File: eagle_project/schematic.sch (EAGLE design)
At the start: 104 parts, among them IC1 AZ34063U, IC2 AZ34063U, IC3 AZ34063U, J1 USB-B, Q1 BC618, Q2 BC618, U1 MCP4912-E/SL, U2 OP07CSZ, U3 OP07CSZ, U4 MCP1501T-40E/CHY, U5 OP07CD, U6 OP07CD, U7 OP07CD

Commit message: schematic mostly done. added mp lab project
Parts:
- removed IC1: AZ34063U, IMPORTED_ELEMENTS:AZ34063U
- removed L3: 100uH, rcl:L-USWE-TPC
- removed L4: 1uH, IMPORTED:INDUCTOR
- removed Q2: BC618, transistor-npn:BC618
- added C21, C22, C23, C25, C26, C28, C29, C30, C31, C32, C38, C40: 100nF, rcl:C-EUC0805
- added C24, C27, C34, C39: 1uF, rcl:C-EUC0805
- added C33: 10uF, rcl:C-EUC0805
- added C35: 220uF/10V/105°, rcl:CPOL-EUE2.5-6
- added C36: 1n, rcl:C-EUC0805
- added C37: 100uF/10V/105°, rcl:CPOL-EUE2-5
- added C41, C42: 10n, rcl:C-EUC0805
- added D3, D4: BAS40, diode:BAS40
- added D5: SS13+, diode:SCHOTTKY-DIODESMC
- added D6, D7: 1N4148, diode:1N4148
- added F1: 1 A, special:FUSE
- added IC4, IC6: LM358A, linear:LM358D
- added IC5: PIC24FJ64GU202-I_SS, SamacSys_Parts:PIC24FJ64GU202-I_SS
- added IC7: AZ34063U, IMPORTED_ELEMENTS:AZ34063U
- added JP10, JP7: PINHD-2X4/90, Connector:PINHD-2X4/90
- added JP11: (no value), pinhead:PINHD-1X4
- added JP8: PINHD-1X5, Connector:PINHD-1X5
- added JP9: PINHD-2X6/90, Connector:PINHD-2X6/90
- added L7: 1mH, SamacSys_Parts:12LRS105C
- added L8: 1uH, IMPORTED:INDUCTOR
- added LED10, LED5, LED6, LED7, LED8, LED9: (no value), led:LEDCHIPLED_0805
- added LED4: (no value), led:LED3MM
- added OK1, OK2, OK4: TR 50%+, optocoupler:LTV816
- added OK3, OK5: ISP521-1X, optocoupler:LTV816
- added R101, R66: 470R, rcl:R-EU_R0805
- added R103, R68: 1K, rcl:R-EU_R0805
- added R104, R105, R62, R67, R70, R77, R78, R79, R81, R82, R84, R87, R97: 1k, rcl:R-EU_R0805
- added R51, R52: 100k 0.1%, rcl:R-EU_R0805
- added R55, R61, R64: 10k, rcl:R-EU_R0805
- added R56, R65: 2k4, rcl:R-EU_R2010
- added R57: 180k 0,1%, rcl:R-EU_R0805
- added R58: 68k 0,1%, rcl:R-EU_R0805
- added R59: 130R 0,1%, rcl:R-EU_R0805
- added R60: 500R, bourns:3362P
- added R69, R96: 160, rcl:R-EU_R0805
- added R71, R98: 510, rcl:R-EU_R0805
- added R72, R73, R74, R75, R76, R91, R92, R93, R94, R99: (no value), pot:TRIM_EU-S64W
- added R80, R95: 220, rcl:R-EU_R0805
- added R83, R85, R89, R90: 1.44k, rcl:R-EU_R0805
- added R86, R88: 3.88k, rcl:R-EU_R0805
- added S1: (no value), switch-omron:10-XX
- added S3: TL36PO, switch:TL36PO
- added T1, T2, T3, T4: (no value), transistor:MMBT3904LT1-NPN-SOT23-BEC
- added TP1, TP2, TP3, TP4, TP5: PTR1PAD1-13, testpad:PTR1PAD1-13
- added U11, U12, U8: OP07CD, IMPORTED:OP07CD
- added U14: MCP4912-E/SL, Microchip_By_element14_Batch_1:MCP4912-E/SL
- added X1, X2, X3: MKDSN1,5/4-5,08, con-phoenix-508:MKDSN1,5/4-5,08
- added X4, X5, X6, X7: MKDSN1,5/2-5,08, con-phoenix-508:MKDSN1,5/2-5,08
- added X8: MKDSN1,5/3-5,08, con-phoenix-508:MKDSN1,5/3-5,08
- C12: value 100uF -> 100uF/25V/105°
- C19, C20: value 1u -> 100nF; device resistor:CPOL-EUE2-5 -> rcl:C-EUC0805
- C3: value 100uF -> 100uF/10V/105°
- C4: value 470uF/10V/105°C+ FOOTPRINT -> 470uF/10V/105°C
- C5: value 100uF/10V/105° -> 220uF/10V/105°; device rcl:CPOL-EUE2-5 -> rcl:CPOL-EUE2.5-6
- C6: value 100nF -> 15pF
- C7: value 1000uF/25V/105° -> 15pF; device rcl:CPOL-EUE5-13 -> rcl:C-EUC0805
- C8: value 1n -> 10uF
- C9: value 100uF -> 10n; device rcl:CPOL-EUE2-5 -> rcl:C-EUC0805
- D1: value SS13+ -> 1N4148; device diode:SCHOTTKY-DIODESMC -> diode:1N4148
- JP1: value PINHD-1X5 -> (none); device Connector:PINHD-1X5 -> pinhead:PINHD-1X4
- JP2: value PINHD-1X5 -> (none); device Connector:PINHD-1X5 -> pinhead:PINHD-1X5
- JP3: value PINHD-2X6/90 -> (none); device Connector:PINHD-2X6/90 -> jumper:JP4E
- JP4: value PINHD-2X4/90 -> (none); device Connector:PINHD-2X4/90 -> jumper:JP4E
- JP5: value PINHD-2X6/90 -> PINHD-1X5; device Connector:PINHD-2X6/90 -> Connector:PINHD-1X5
- JP6: value PINHD-2X4/90 -> PINHD-2X6/90; device Connector:PINHD-2X4/90 -> Connector:PINHD-2X6/90
- L1, L5: value 100uH -> 1mH; device rcl:L-USWE-TPC -> SamacSys_Parts:12LRS105C
- LED2: device led:LED3MM -> led:LEDCHIPLED_0805
- Q1: value BC618 -> 16MHz; device transistor-npn:BC618 -> crystal:CRYSTALHC49U-V
- R10: value 1k -> 180k 0,1%; device resistor:R-EU_0207/7 -> rcl:R-EU_R0805
- R11: value 1k -> 68k 0,1%; device resistor:R-EU_0207/7 -> rcl:R-EU_R0805
- R12: value 1.44k -> 500R; device resistor:R-EU_0207/7 -> bourns:3362P
- R13: value 1k -> 137k; device resistor:R-EU_0207/7 -> rcl:R-EU_R0805
- R14: value 1.44k -> 1k; device resistor:R-EU_0207/7 -> bourns:3362P
- R15: value 1k -> 1M; device resistor:R-EU_0207/7 -> rcl:R-EU_R0805
- R16: value 3.88k -> 137k; device resistor:R-EU_0207/7 -> rcl:R-EU_R0805
- R17: value 160 -> 1k; device resistor:R-EU_0207/7 -> bourns:3362P
- R18: value 1k -> 150k; device resistor:R-EU_0207/7 -> rcl:R-EU_R0805
- R19: value 510 -> 82k; device resistor:R-EU_0207/7 -> rcl:R-EU_R0805
- R20: value 220 -> (none); device resistor:R-EU_0207/7 -> pot:TRIM_EU-S64W
- R21: value 1k -> 10k; device resistor:R-EU_0207/7 -> rcl:R-EU_R0805
- R22: device resistor:R-EU_0207/7 -> rcl:R-EU_R0805
- R23: value 1.44k -> 10k; device resistor:R-EU_0207/7 -> rcl:R-EU_R0805
- R24: value 1k -> (none); device resistor:R-EU_0207/7 -> rcl:R-EU_R0805
- R25: value 1.44k -> 3k3; device resistor:R-EU_0207/7 -> rcl:R-EU_R0805
- R26: value 1k -> 2k; device resistor:R-EU_0207/7 -> rcl:R-EU_R0805
- R27: value 3.88k -> 0R75; device resistor:R-EU_0207/7 -> rcl:R-EU_R0805
- R28: value 160 -> 47R; device resistor:R-EU_0207/7 -> rcl:R-EU_M0805
- R30: value (none) -> 100k; device rcl:R-EU_R0805 -> rcl:R-EU_M0805
- R31: value 33k -> 10k
- R32: value 3k9 -> 2k4; device rcl:R-EU_R0805 -> rcl:R-EU_R2010
- R33: value 0R24 -> 10k
- R34: value 75R -> 1k
- R38: value 0R24 -> 0R39
- R39: value 1k -> (none); device resistor:R-EU_0207/7 -> pot:TRIM_EU-S64W
- R40: value 510 -> 22k 0.1%; device resistor:R-EU_0207/7 -> rcl:R-EU_R0805
- R41: value (none) -> 91k 0.1%; device pot:TRIM_EU-S64W -> rcl:R-EU_R0805
- R43, R44, R45, R46, R49, R50: value (none) -> 100k 0.1%; device pot:TRIM_EU-S64W -> rcl:R-EU_R0805
- R47: value (none) -> 130R 0,1%; device pot:TRIM_EU-S64W -> rcl:R-EU_R0805
- R53: value 3k3 -> 10k
- R54: value 2k -> 3k3
- R63: value 1R5 -> 0R75
- R9: value 220 -> 1M; device resistor:R-EU_0207/7 -> rcl:R-EU_R0805
- U1: value MCP4912-E/SL -> OP07CD; device Microchip_By_element14_Batch_1:MCP4912-E/SL -> IMPORTED:OP07CD
- U2, U3: value OP07CSZ -> OP07CD; device Analog Devices_By_element14_Batch_1:OP07CSZ -> IMPORTED:OP07CD
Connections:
- removed net +5V1: C7.+, D1.C, L4.1, R31.2
- removed net D+: J1.3
- removed net D-: J1.2
- new net +5V3: C35.+, L5.2, L8.1, R25.2
- new net 1,451: IC4A.+IN, IC4B.+IN, TP5.TP, U1.IN-, U1.OUT
- new net AREF_3,3: D3.C, D4.C, IC5.PGED3/VREF+/CVREF+/AN0/C3INC/RP26/ASDA1/RA0, TP3.TP, U11.IN-, U11.OUT
- new net COM: OK3.EMIT, OK5.EMIT, X8-3.KL
- new net COM_IN_1_3,3: JP11.4
- new net COM_IN_2_3,3: JP1.4
- new net D+_PGD: IC5.PGED2/RP10/D+/RB10, J1.3, JP2.4
- new net D-_PGC: IC5.PGEC2/RP11/D-/RB11, J1.2, JP2.5
- new net D_IN_0: IC5.AN4/C1INB/RP2/SDA2/RB2, LED2.C, OK4.COL, R31.1
- new net D_IN_1: IC5.AN5/C1INA/RP3/SCL2/RB3, LED5.C, OK1.COL, R55.1
- new net D_IN_2: IC5.SOSCI/C2IND/RP4/RB4, LED6.C, OK2.COL, R64.1
- new net D_OUT_0: IC5.SOSCO/SCLKI/C2INC/PWRLCLK/RA4, T1.B
- new net D_OUT_1: IC5.TMS/RP5/USBID/RB5, T2.B
- new net I_IN_0_3,3: D3.A, IC5.PGED1/AN2/LVDIN/C2INB/RP0/RB0, JP11.1, R46.2, U8.OUT
- new net I_IN_1_+: JP4.3, X1-1.KL
- new net I_IN_1_-: X1-2.KL
- new net I_IN_1_3,3: D4.A, IC5.PGEC1/AN1-/AN3/C2INA/RP1/RB1, JP1.1, R52.2, U12.OUT
- new net I_IN_2_+: JP3.3, X1-3.KL
- new net I_IN_2_-: X1-4.KL
- new net MCLR: IC5.!MCLR, JP2.1, R23.1, S1.S, S1.S1
- new net N$100: JP9.8, R93.A, R93.S
- new net N$101: JP9.10, R94.A, R94.S
- new net N$102: R83.1, R92.E
- new net N$103: R85.1, R93.E
- new net N$104: R86.1, R94.E
- new net N$105: JP6.8, R74.A, R74.S
- new net N$106: JP6.10, R75.A, R75.S
- new net N$107: R73.E, R90.1
- new net N$108: R74.E, R89.1
- new net N$109: R99.E, U2.OFFSETN1
- new net N$110: R75.E, R88.1
- new net N$111: R76.A, U3.OFFSETN2
- new net N$112: R76.E, U3.OFFSETN1
- new net N$113: OK5.A, R101.2
- new net N$114: OK5.COL, X8-2.KL
- new net N$116: LED8.A, R103.1
- new net N$117: C33.1, IC5.VCAP
- new net N$118: LED8.C, OK5.C, T2.C
- new net N$119: LED9.A, R104.1
- new net N$120: LED10.A, R105.1
- new net N$65: U3.IN-
- new net N$66: U14.VOUTB, U2.IN-
- new net N$67: R97.1, T4.B
- new net N$68: JP7.4, R96.1, T4.E
- new net N$71: JP6.3, R79.1, R95.2
- new net N$72: JP6.7, R77.1, R89.2
- new net N$73: JP6.9, R87.1, R88.2
- new net N$74: JP6.5, R78.1, R90.2
- new net N$75: JP7.1, U3.IN+
- new net N$76: JP6.1, JP7.3
- new net N$77: JP6.2, JP7.5
- new net N$78: JP7.6, R97.2
- new net N$79: R72.E, R95.1
- new net N$80: JP6.6, R73.A, R73.S
- new net N$81: JP6.4, R72.A, R72.S
- new net N$84: R70.1, T3.B
- new net N$85: JP10.4, R69.1, T3.E
- new net N$86: JP9.3, R80.2, R84.1
- new net N$87: JP9.7, R81.1, R85.2
- new net N$88: JP9.9, R67.1, R86.2
- new net N$89: JP4.2, R45.2, R59.2
- new net N$90: JP9.5, R82.1, R83.2
- new net N$91: JP10.1, U2.IN+
- new net N$92: JP10.3, JP9.1
- new net N$93: IC6B.-IN, IC6B.OUT, R57.1
- new net N$94: JP10.5, JP9.2
- new net N$95: JP10.6, R70.2
- new net N$96: R43.1, R59.1
- new net N$97: R80.1, R91.E
- new net N$98: JP9.6, R92.A, R92.S
- new net N$99: JP9.4, R91.A, R91.S
- new net OSCI: C6.1, IC5.OSCI/CLKI/C1IND/RA2, Q1.1
- new net OSCO: C7.1, IC5.OSCO/CLKO/C2IND/RA3, Q1.2
- new net PROG: R105.2, S3.O
- new net RUN: R104.2, S3.S
- new net VBUS: IC5.VBUS/RB6, R28.2, R30.2
- new net VCC: R101.1, R103.2, R66.1, R68.2, S3.P
- new net VDD2: C38.1
- new net V_IN_-10-+10_0_3,3: IC4A.OUT, IC5.CVREF/AN6/C3INB/RP14/RB14, JP1.3, JP11.3, R17.2, R17.3
- new net V_IN_-10-+10_1_3,3: IC4B.OUT, IC5.AN7/C1INC/RP13/_RB13, R14.2, R14.3
- new net V_IN_0-10_0_3,3: IC5.PGEC3/CVREF-/AN1/C3IND/RP27/ASCL1/RA1, JP1.2, JP11.2, R10.2, R12.1
- new net V_IN_0-10_1_3,3: IC5.AN9/C3INA/RP15/RB15, R57.2, R60.1
- new net V_IN_1_-10-+10_+: R15.1, X2-1.KL
- new net V_IN_1_0-10_+: IC6A.+IN, X3-1.KL
- new net V_IN_2_-10-+10_+: R9.1, X2-3.KL
- new net V_IN_2_0-10_+: IC6B.+IN, X3-3.KL
- net +12V: now also C2.1, C22.1, C26.1, C28.1, C31.1, C39.1, C4.+, F1.2, IC2.VCC, IC3.VCC, IC4P.V+, IC6P.V+, IC7.VCC, JP3.4, JP4.4, R27.1, R38.1, R63.1, R71.1, R76.S, R98.1, R99.S, U2.VCC+, U3.VCC+; no longer C9.+, L4.2, R19.1, R30.2, R40.1, U2.V+, U3.V+
- net +3V3: now also C37.+, C40.1, C8.1, IC5.AVDD/VDD, IC5.VDD, IC5.VUSB3V3, JP2.2, L8.2, R23.2, R24.2; no longer C3.+, L2.2, R29.2
- net +5V: now also C41.1, C42.1, C9.1, OK1.A, OK2.A, OK4.A, R21.2, R22.2, R31.2, R33.2, R34.2, R55.2, R61.2, R62.2, R64.2, X5-1.KL, X6-1.KL, X7-1.KL
- net -12V: now also C25.1, C29.1, C32.1, IC4P.V-, U2.VCC-, U3.VCC-; no longer U2.V-, U3.V-
- net 2,577: now also R67.2, R87.2, TP2.TP; no longer R15.1, R26.1
- net 3,472: now also R78.2, R82.2, TP1.TP; no longer R11.1, R22.1
- net 4,096: now also R18.2, R40.2, TP4.TP, U14.VREFA, U14.VREFB; no longer U1.VREFA, U1.VREFB
- net CS_DAC1: now also IC5.TDO/C1INC/C2INC/C3INC/RP9/SDA1/_T1CK/RB9, U14.*CS; no longer U1.*CS
- net GND: now also C19.1, C20.1, C21.1, C22.2, C23.1, C24.2, C25.2, C26.2, C27.2, C28.2, C29.2, C30.2, C31.2, C32.2, C33.2, C34.2, C35.-, C36.2, C37.-, C38.2, C39.2, C40.2, C7.2, D5.A, IC5.AVSS/VSS, IC5.VSS_1, IC5.VSS_2, IC6P.V-, IC7.GND, JP10.7, JP10.8, JP2.3, JP3.1, JP4.1, JP6.11, JP6.12, JP7.7, JP7.8, JP9.11, JP9.12, L7.2, LED10.C, LED4.C, LED9.C, OK1.EMIT, OK2.EMIT, OK4.EMIT, R11.2, R19.1, R26.1, R30.1, R41.1, R44.1, R50.1, R58.2, R69.2, R77.2, R79.2, R81.2, R84.2, R96.2, S1.P, S1.P1, T1.E, T2.E, U1.VCC-, U11.VCC-, U12.VCC-, U14.*LDAC, U14.VSS, U8.VCC-, X2-2.KL, X2-4.KL, X3-2.KL, X3-4.KL, X4-2.KL; no longer C19.-, C20.-, C7.-, C9.-, IC1.GND, IC1.SWE, JP3.11, JP3.12, JP4.7, JP4.8, JP5.11, JP5.12, JP6.7, JP6.8, L5.2, LED2.C, R10.1, R13.1, R17.1, R21.1, R24.1, R28.1, R32.1, U1.*LDAC, U1.VSS
- net I+: now also C24.1, C27.1, JP5.1, JP8.1, R71.2, R98.2; no longer C19.+, C20.+, JP1.1, JP2.1, R19.2, R40.2
- net I-: now also JP5.2, JP8.2, T3.C, T4.C; no longer JP1.2, JP2.2, Q1.C, Q2.C
- net MOSI: now also IC5.TCK/RP8/SCL1/!USBOEN!/RB8, U14.SDI; no longer U1.SDI
- net N$11: now also LED4.A, R24.1; no longer JP3.3, R10.2, R9.1
- net N$12: now also C34.1, J1.1, R28.1; no longer JP3.7, R13.2, R14.1
- net N$13: now also C9.2, D1.A, OK4.C, R21.1; no longer JP3.9, R15.2, R16.1
- net N$14: now also R16.2, R17.1; no longer JP3.5, R11.2, R12.1
- net N$16: now also R22.1; no longer R30.1
- net N$17: now also R32.1, X5-2.KL; no longer IC1.COMP_INV_IN, R31.1, R32.2
- net N$18: now also OK3.A, R66.2; no longer IC1.IPK_SENSE, L3.1, R33.2, R34.1
- net N$20: now also IC4A.-IN, R15.2, R16.1; no longer U1.VOUTA, U2.+IN
- net N$21: now also D1.C, R32.2; no longer C8.1, IC1.TC
- net N$22: now also F1.1, X4-1.KL; no longer Q1.B, R18.2
- net N$23: now also R18.1, R19.2, U1.IN+; no longer JP3.4, R45.A, R45.S
- net N$24: now also R20.A, U1.OFFSETN2; no longer U1.VOUTB, U3.+IN
- net N$25: now also IC6A.-IN, IC6A.OUT, R10.1; no longer JP4.4, Q1.E, R17.2
- net N$26: now also R11.1, R12.2, R12.3; no longer JP3.6, R46.A, R46.S
- net N$27: now also R20.E, U1.OFFSETN1; no longer JP3.8, R47.A, R47.S
- net N$28: now also IC4B.-IN, R13.1, R9.2; no longer JP3.10, R48.A, R48.S
- net N$29: now also C41.2, D6.A, OK1.C, R33.1; no longer IC1.DRVC, R34.2
- net N$30: now also LED5.A, R34.1; no longer D1.A, IC1.SWC, L3.2
- net N$32: now also IC7.COMP_INV_IN, R25.1, R26.2; no longer JP4.1, U2.-IN
- net N$35: now also R13.2, R14.1; no longer JP3.1, JP4.3
- net N$36: now also R56.1, X6-2.KL; no longer JP3.2, JP4.5
- net N$37: now also OK3.COL, X8-1.KL; no longer Q2.B, R39.2
- net N$38: now also IC7.DRVC, IC7.IPK_SENSE, IC7.SWC, R27.2; no longer JP6.4, Q2.E, R28.2
- net N$39: now also D6.C, R56.2; no longer JP5.3, R20.1, R21.2
- net N$40: now also R40.1, R41.2, U11.IN+; no longer JP4.6, R18.1
- net N$41: now also R39.A, U8.OFFSETN2; no longer JP5.7, R24.2, R25.1
- net N$42: now also L7.1; no longer L5.1
- net N$43: now also R39.E, U8.OFFSETN1; no longer JP5.9, R26.2, R27.1
- net N$44: now also R42.A, U11.OFFSETN2; no longer JP5.5, R22.2, R23.1
- net N$45: now also R42.E, U11.OFFSETN1; no longer JP5.8, R43.A, R43.S
- net N$46: now also R45.1, R46.1, U8.IN-; no longer R23.2, R41.E
- net N$47: now also R43.2, R44.2, U8.IN+; no longer R45.E, R9.2
- net N$48: now also JP3.2, R47.2, R51.2; no longer R49.A, U3.VOS_TRIM
- net N$49: now also R47.1, R49.1; no longer JP6.1, U3.-IN
- net N$50: now also R48.A, U12.OFFSETN2; no longer JP5.1, JP6.3
- net N$51: now also R48.E, U12.OFFSETN1; no longer JP5.2, JP6.5
- net N$52: now also R51.1, R52.1, U12.IN-; no longer JP6.6, R39.1
- net N$53: now also R49.2, R50.2, U12.IN+; no longer R20.2, R42.E
- net N$54: now also C42.2, D7.A, OK2.C, R61.1; no longer JP5.6, R41.A, R41.S
- net N$55: now also R58.1, R60.2, R60.3; no longer JP5.4, R42.A, R42.S
- net N$56: now also LED6.A, R62.1; no longer R25.2, R43.E
- net N$57: now also R65.1, X7-2.KL; no longer JP5.10, R44.A, R44.S
- net N$58: now also D5.C, IC7.SWE, L5.1; no longer R27.2, R44.E
- net N$59: now also R99.A, U2.OFFSETN2; no longer R49.E, U3.VOS_TRIM_2
- net N$60: now also C36.1, IC7.TC; no longer R50.A, U2.VOS_TRIM
- net N$61: now also D7.C, R65.2; no longer R50.E, U2.VOS_TRIM_2
- net N$62: now also LED7.A, R68.1; no longer R12.2, R46.E
- net N$63: now also LED7.C, OK3.C, T1.C; no longer R14.2, R47.E
- net N$64: now also U14.VOUTA; no longer R16.2, R48.E
- net SCK: now also IC5.TDI/RP7/INT0/RB7, U14.SCK; no longer U1.SCK
- net V+: now also JP10.2, JP5.3, JP7.2, JP8.3; no longer JP1.3, JP2.3, JP4.2, JP6.2
- net V-: now also JP5.4, JP5.5, JP8.4, JP8.5; no longer JP1.4, JP1.5, JP2.4, JP2.5
- net VDD: now also C19.2, C20.2, C21.2, C23.2, C3.+, C30.1, L2.2, R20.S, R29.2, R39.S, R42.S, R48.S, U1.VCC+, U11.VCC+, U12.VCC+, U14.*SHDN, U14.VDD, U8.VCC+; no longer C2.1, C4.+, C6.1, IC1.VCC, IC2.VCC, IC3.VCC, J1.1, R33.1, R38.1, R49.S, R50.S, R63.1, U1.*SHDN, U1.VDD
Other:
- note added: "-10...10 V"
- note added: "0...10 V"
- note added: "0...20 mA"
- note added: "1"
- note added: "1P3T"
- note added: "2"
- note added: "3"
- note added: "4"
- note added: "IZHOD"
- note added: "Izbira napetostnega območja 2P4T"
- note added: "Izbira tok ali napetost 2P2T"
- note added: "Loop-powered"
- note added: "Samo upor"
- note added: "max +/- 12V"
- note added: "max +12V"
- note added: "max 24 mA"

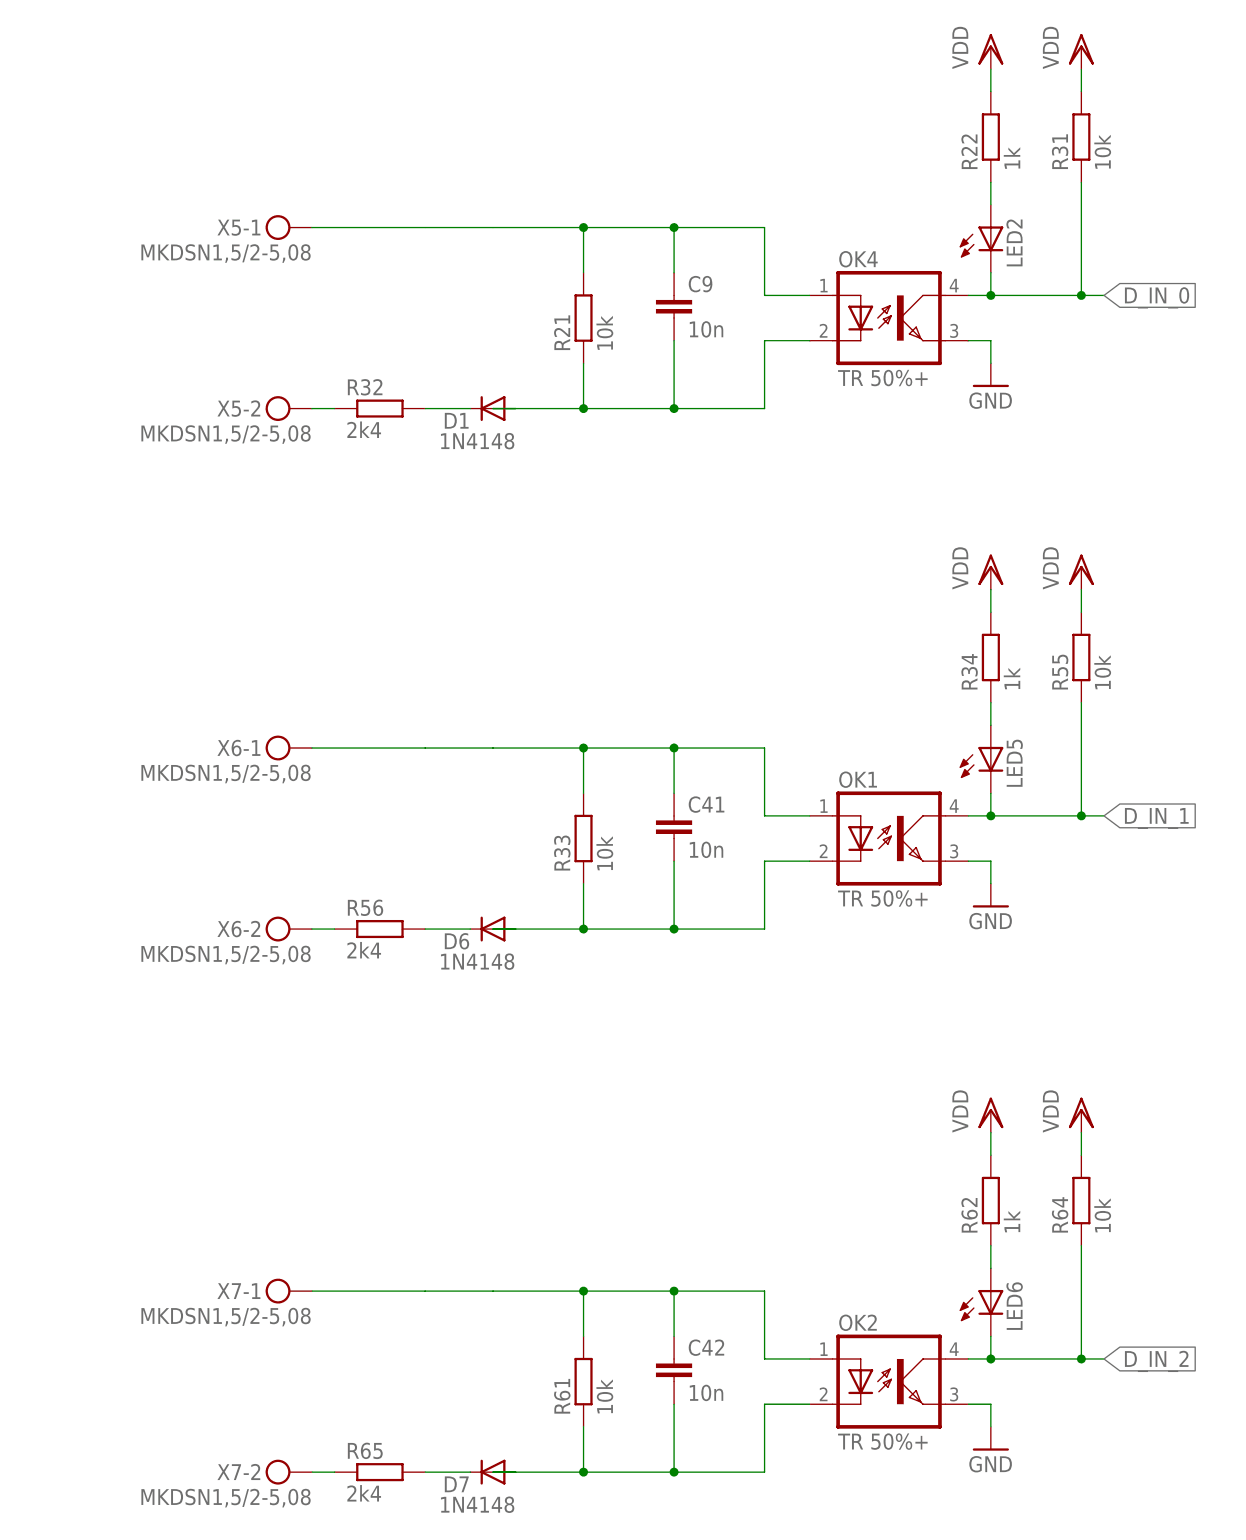
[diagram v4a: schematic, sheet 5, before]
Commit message: changed R values in AO and changed DI
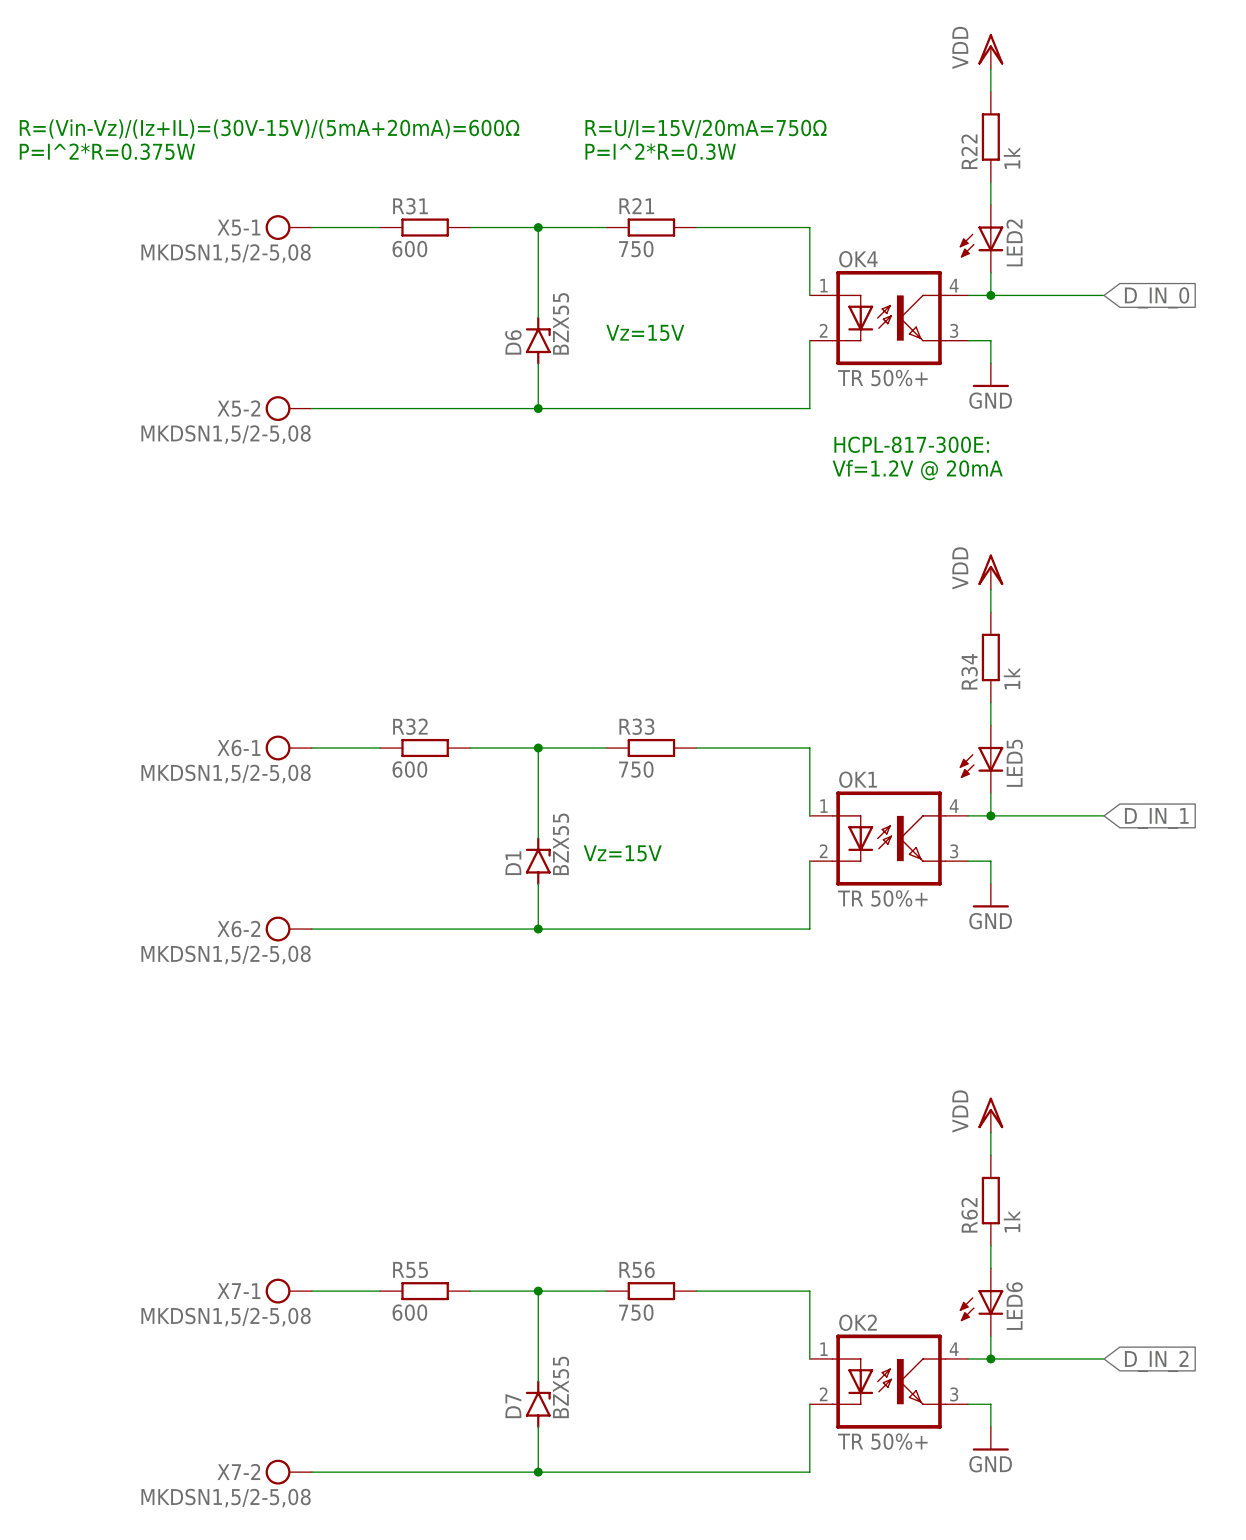
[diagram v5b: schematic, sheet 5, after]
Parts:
- removed C41, C42, C9: 10n, rcl:C-EUC0805
- removed JP10, JP7: PINHD-2X4/90, Connector:PINHD-2X4/90
- removed JP5, JP8: PINHD-1X5, Connector:PINHD-1X5
- removed JP6, JP9: PINHD-2X6/90, Connector:PINHD-2X6/90
- removed R61, R64: 10k, rcl:R-EU_R0805
- removed R65: 2k4, rcl:R-EU_R2010
- removed R70, R97: 1k, rcl:R-EU_R0805
- added JP12, JP13: (no value), pinhead:PINHD-2X4
- added JP14, JP15: (no value), pinhead:PINHD-2X6
- added JP16, JP17: (no value), pinhead:PINHD-1X5
- D1, D6, D7: value 1N4148 -> BZX55; device diode:1N4148 -> diode:BZX55
- R21, R33: value 10k -> 750; device rcl:R-EU_R0805 -> rcl:R-EU_0309/12
- R31, R55: value 10k -> 600; device rcl:R-EU_R0805 -> rcl:R-EU_0309/12
- R32: value 2k4 -> 600; device rcl:R-EU_R2010 -> rcl:R-EU_0309/12
- R56: value 2k4 -> 750; device rcl:R-EU_R2010 -> rcl:R-EU_0309/12
- R67, R77, R78, R79, R81, R82, R84, R87: value 1k -> 100k
- R80, R95: value 220 -> 22k
- R83, R85, R89, R90: value 1.44k -> 144k
- R86, R88: value 3.88k -> 388k
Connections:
- new net N$115: OK4.A, R21.2
- net +5V: no longer C41.1, C42.1, C9.1, OK1.A, OK2.A, OK4.A, R21.2, R31.2, R33.2, R55.2, R61.2, R64.2, X5-1.KL, X6-1.KL, X7-1.KL
- net D_IN_0: no longer R31.1
- net D_IN_1: no longer R55.1
- net D_IN_2: no longer R64.1
- net GND: now also JP12.7, JP12.8, JP13.7, JP13.8, JP14.11, JP14.12, JP15.11, JP15.12; no longer JP10.7, JP10.8, JP6.11, JP6.12, JP7.7, JP7.8, JP9.11, JP9.12
- net I+: now also JP16.1, JP17.1; no longer JP5.1, JP8.1
- net I-: now also JP16.2, JP17.2; no longer JP5.2, JP8.2
- net N$100: now also JP15.8; no longer JP9.8
- net N$101: now also JP15.10; no longer JP9.10
- net N$105: now also JP14.8; no longer JP6.8
- net N$106: now also JP14.10; no longer JP6.10
- net N$13: now also R32.1, X6-1.KL; no longer C9.2, D1.A, OK4.C, R21.1
- net N$17: now also D1.A, OK1.C, X6-2.KL; no longer R32.1, X5-2.KL
- net N$21: now also R33.1
- net N$29: now also OK1.A, R33.2; no longer C41.2, D6.A, OK1.C, R33.1
- net N$36: now also R31.1, X5-1.KL; no longer R56.1, X6-2.KL
- net N$39: now also D6.A, OK4.C, X5-2.KL; no longer D6.C, R56.2
- net N$54: now also R55.1, X7-1.KL; no longer C42.2, D7.A, OK2.C, R61.1
- net N$57: now also D7.A, OK2.C; no longer R65.1
- net N$61: now also R55.2, R56.1; no longer R65.2
- net N$67: now also OK2.A, R56.2; no longer R97.1, T4.B
- net N$68: now also JP13.4; no longer JP7.4
- net N$71: now also JP14.3; no longer JP6.3
- net N$72: now also JP14.7; no longer JP6.7
- net N$73: now also JP14.9; no longer JP6.9
- net N$74: now also JP14.5; no longer JP6.5
- net N$75: now also JP13.1; no longer JP7.1
- net N$76: now also JP13.3, JP14.1; no longer JP6.1, JP7.3
- net N$77: now also JP13.5, JP14.2; no longer JP6.2, JP7.5
- net N$78: now also JP13.6, T4.B; no longer JP7.6, R97.2
- net N$80: now also JP14.6; no longer JP6.6
- net N$81: now also JP14.4; no longer JP6.4
- net N$84: now also D6.C, R21.1, R31.2; no longer R70.1, T3.B
- net N$85: now also JP12.4; no longer JP10.4
- net N$86: now also JP15.3; no longer JP9.3
- net N$87: now also JP15.7; no longer JP9.7
- net N$88: now also JP15.9; no longer JP9.9
- net N$90: now also JP15.5; no longer JP9.5
- net N$91: now also JP12.1; no longer JP10.1
- net N$92: now also JP12.3, JP15.1; no longer JP10.3, JP9.1
- net N$94: now also JP12.5, JP15.2; no longer JP10.5, JP9.2
- net N$95: now also JP12.6, T3.B; no longer JP10.6, R70.2
- net N$98: now also JP15.6; no longer JP9.6
- net N$99: now also JP15.4; no longer JP9.4
- net V+: now also JP12.2, JP13.2, JP16.3, JP17.3; no longer JP10.2, JP5.3, JP7.2, JP8.3
- net V-: now also JP16.4, JP16.5, JP17.4, JP17.5; no longer JP5.4, JP5.5, JP8.4, JP8.5
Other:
- note added: "HCPL-817-300E: Vf=1.2V @ 20mA"
- note added: "Pri 25mA bo ΔU=4V P=I^2*R=0.1W"
- note added: "R=(Vin-Vz)/(Iz+IL)=(30V-15V)/(5mA+20mA)=600Ω P=I^2*R=0.375W"
- note added: "R=U/I=15V/20mA=750Ω P=I^2*R=0.3W"
- note added: "Vz=15V"
- note removed: "Pri 25mA bo ΔU=4V"
- moved on the sheet: R21, R31, R32, R33, R55, R56
